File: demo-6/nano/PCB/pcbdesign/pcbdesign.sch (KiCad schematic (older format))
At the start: 18 parts, among them J1 Relay, J2 12v input, J3 Encoder, J4 HC-SR04, J5 Display, J6 InflowPump, J7 Outflow Switch, J8 Outflow Pump, Q1 PN2222A

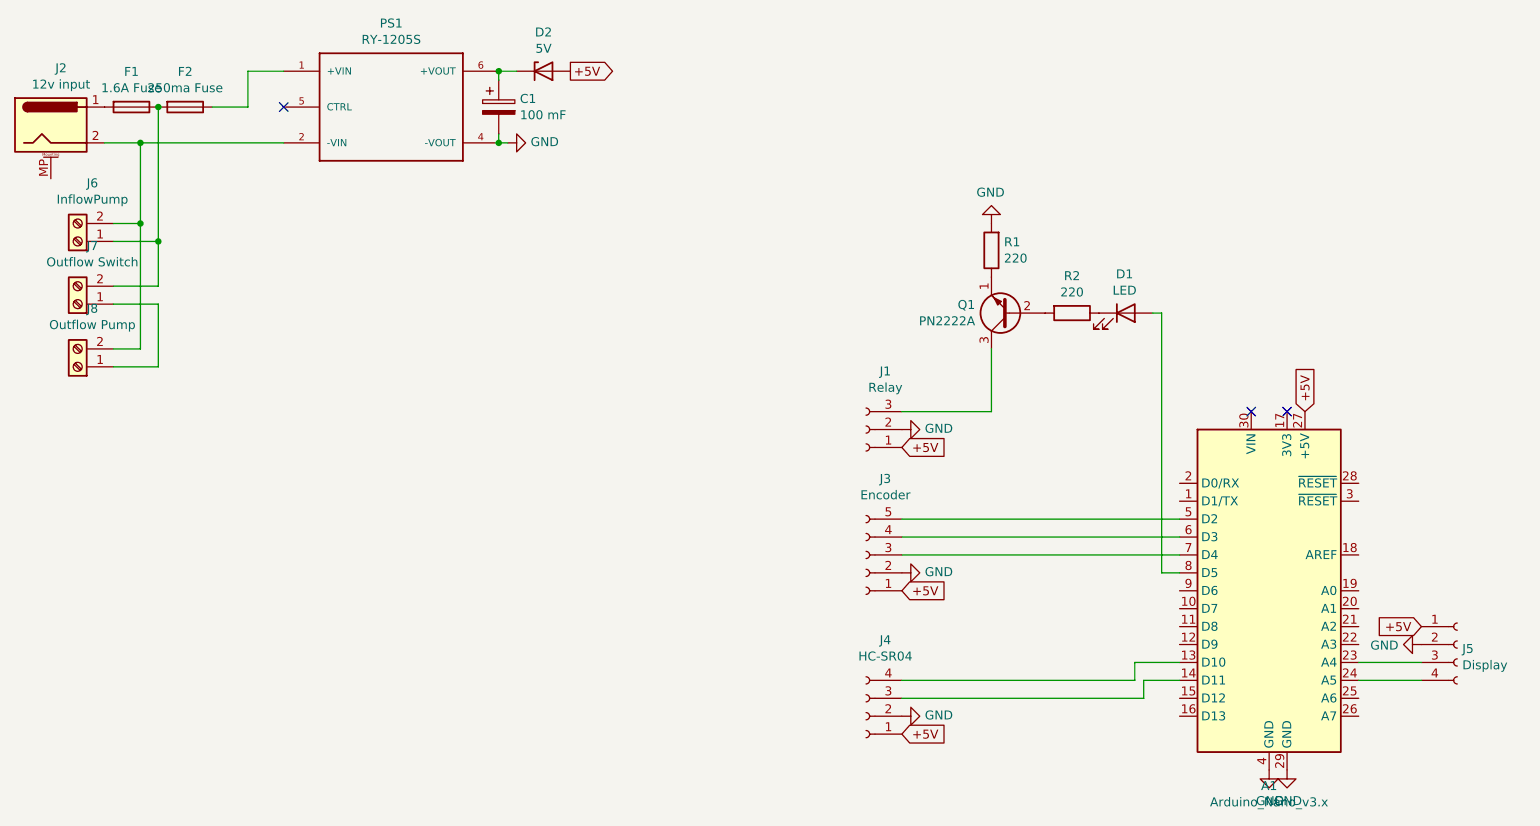
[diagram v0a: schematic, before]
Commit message: adding some schematics
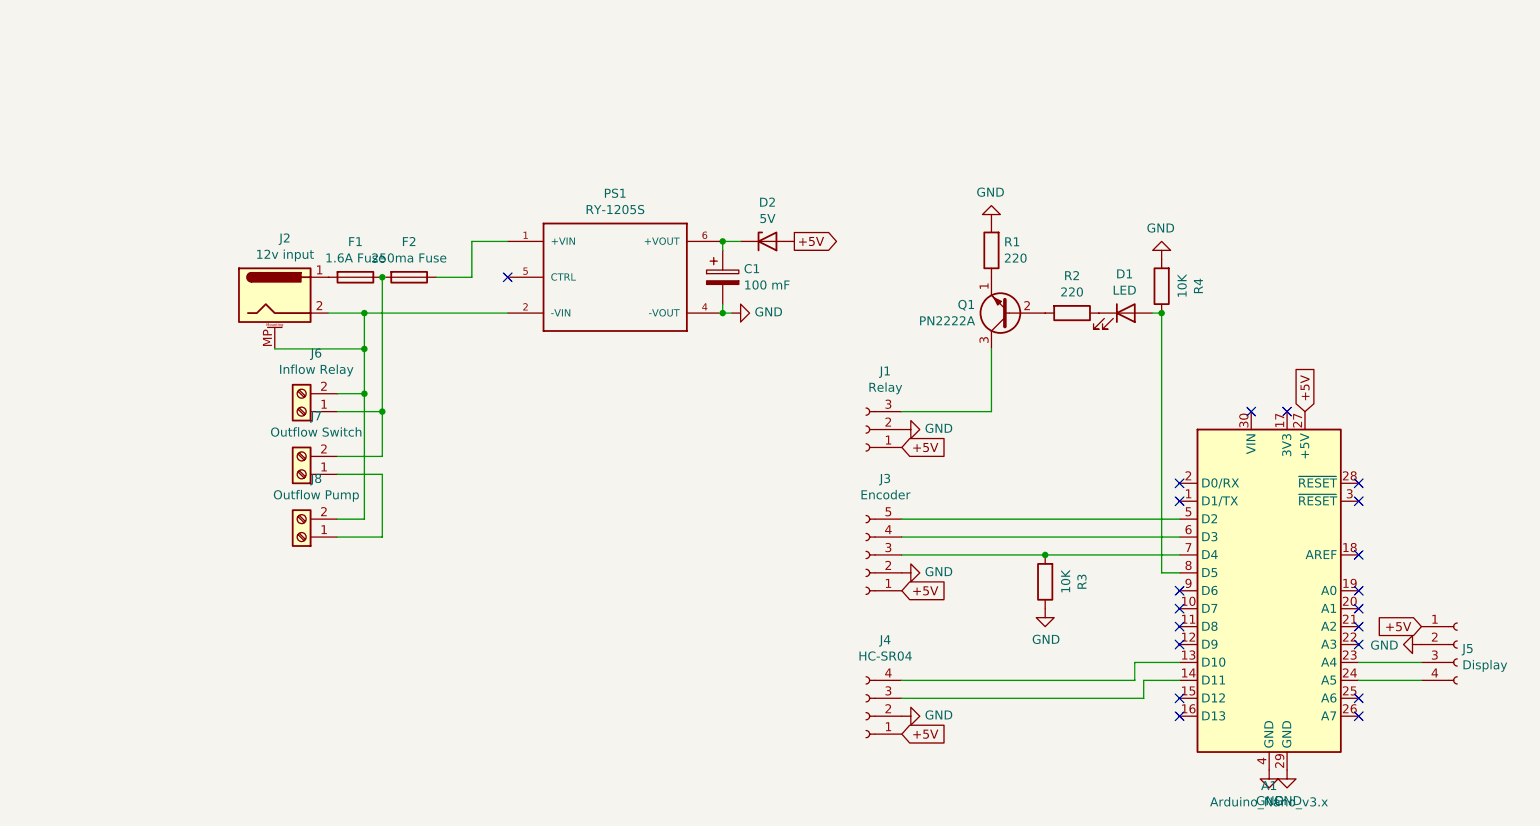
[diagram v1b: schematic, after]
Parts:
- added R3, R4: 10K, Resistor_THT:R_Axial_DIN0207_L6.3mm_D2.5mm_P7.62mm_Horizontal, symbol Device:R
- C1: footprint (none) -> Capacitor_THT:CP_Radial_D8.0mm_P3.50mm
- D1: footprint (none) -> LED_THT:LED_D4.0mm
- D2: footprint (none) -> Diode_THT:D_A-405_P7.62mm_Horizontal
- F1, F2: footprint (none) -> Fuse:Fuseholder_Cylinder-6.3x32mm_Schurter_0031-8002_Horizontal_Open
- J1: footprint (none) -> Connector_PinSocket_2.54mm:PinSocket_1x03_P2.54mm_Vertical
- J4, J5: footprint (none) -> Connector_PinSocket_2.54mm:PinSocket_1x04_P2.54mm_Vertical
- J6: value InflowPump -> Inflow Relay; footprint (none) -> TerminalBlock:TerminalBlock_bornier-2_P5.08mm
- J7, J8: footprint (none) -> TerminalBlock:TerminalBlock_bornier-2_P5.08mm
- PS1: footprint CONV_RY-1205S -> RY-1205S:CONV_RY-1205S
- R1, R2: footprint (none) -> Resistor_THT:R_Axial_DIN0207_L6.3mm_D2.5mm_P7.62mm_Horizontal
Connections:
- net GND: now also R3.1, R4.2
- net at A1.7 (D4), J3.3 (Pin_3): now also R3.2
- net at A1.8 (D5), D1.2 (A): now also R4.1
- net at J2.2, J6.2 (Pin_2), J8.2 (Pin_2)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: now also J2.MP (MountPin)
- no-connect marks 3 -> 20
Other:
- moved on the sheet: C1, D2, F1, F2, J2, J6, J7, J8

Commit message: ready for pcb
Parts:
- J2: footprint Connector_BarrelJack:BarrelJack_Wuerth_6941xx301002 -> Connector_BarrelJack:BarrelJack_CUI_PJ-063AH_Horizontal
- J3: footprint Connector_BarrelJack:BarrelJack_Horizontal -> Connector_PinSocket_2.54mm:PinSocket_1x05_P2.54mm_Vertical
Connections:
- net at A1.8 (D5), D1.2 (A): no longer R4.1
- net at D1.1 (K), R2.1: now also R4.1
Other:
- moved on the sheet: R4
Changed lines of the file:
@@
 F 0 "J3" H 6142 3475 50  0000 C CNN
 F 1 "Encoder" H 6142 3566 50  0000 C CNN
-F 2 "Connector_BarrelJack:BarrelJack_Horizontal" H 6250 3900 50  0001 C CNN
+F 2 "Connector_PinSocket_2.54mm:PinSocket_1x05_P2.54mm_Vertical" H 6250 3900 50  0001 C CNN
 F 3 "~" H 6250 3900 50  0001 C CNN
 	1    6250 3900
@@
 	0    -1   -1   0
 $EndComp
-$Comp
-L Connector:Conn_01x04_Female J5
-U 1 1 5F4E310F
-P 9550 4400
-F 0 "J5" H 9578 4376 50  0000 L CNN
-F 1 "Display" H 9578 4285 50  0000 L CNN
-F 2 "Connector_PinSocket_2.54mm:PinSocket_1x04_P2.54mm_Vertical" H 9550 4400 50  0001 C CNN
-F 3 "~" H 9550 4400 50  0001 C CNN
-	1    9550 4400
-	1    0    0    -1
-$EndComp
 Wire Wire Line
 	9350 4600 9000 4600
@@
 F 0 "J2" H 3007 2767 50  0000 C CNN
 F 1 "12v input" H 3007 2676 50  0000 C CNN
-F 2 "Connector_BarrelJack:BarrelJack_Wuerth_6941xx301002" H 3000 2410 50  0001 C CNN
+F 2 "Connector_BarrelJack:BarrelJack_CUI_PJ-063AH_Horizontal" H 3000 2410 50  0001 C CNN
 F 3 "~" H 3000 2410 50  0001 C CNN
 	1    2950 2450
@@
 L power:GND #PWR03
 U 1 1 5F4E5570
-P 7900 2250
-F 0 "#PWR03" H 7900 2000 50  0001 C CNN
-F 1 "GND" H 7905 2077 50  0000 C CNN
-F 2 "" H 7900 2250 50  0001 C CNN
-F 3 "" H 7900 2250 50  0001 C CNN
-	1    7900 2250
-	-1   0    0    1
-$EndComp
-Connection ~ 7900 2550
+P 7550 2250
+F 0 "#PWR03" H 7550 2000 50  0001 C CNN
+F 1 "GND" H 7555 2077 50  0000 C CNN
+F 2 "" H 7550 2250 50  0001 C CNN
+F 3 "" H 7550 2250 50  0001 C CNN
+	1    7550 2250
+	-1   0    0    1
+$EndComp
 $Comp
 L Device:R R4
 U 1 1 5F4E50D6
-P 7900 2400
-F 0 "R4" V 7693 2400 50  0000 C CNN
-F 1 "10K" V 7784 2400 50  0000 C CNN
-F 2 "Resistor_THT:R_Axial_DIN0207_L6.3mm_D2.5mm_P7.62mm_Horizontal" V 7830 2400 50  0001 C CNN
-F 3 "~" H 7900 2400 50  0001 C CNN
-	1    7900 2400
+P 7550 2400
+F 0 "R4" V 7343 2400 50  0000 C CNN
+F 1 "10K" V 7434 2400 50  0000 C CNN
+F 2 "Resistor_THT:R_Axial_DIN0207_L6.3mm_D2.5mm_P7.62mm_Horizontal" V 7480 2400 50  0001 C CNN
+F 3 "~" H 7550 2400 50  0001 C CNN
+	1    7550 2400
 	-1   0    0    1
 $EndComp
@@
 Connection ~ 5450 2150
 Connection ~ 5450 2550
+Connection ~ 7550 2550
+$Comp
+L Connector:Conn_01x04_Female J5
+U 1 1 5F4E310F
+P 9550 4400
+F 0 "J5" H 9578 4376 50  0000 L CNN
+F 1 "Display" H 9578 4285 50  0000 L CNN
+F 2 "Connector_PinSocket_2.54mm:PinSocket_1x04_P2.54mm_Vertical" H 9550 4400 50  0001 C CNN
+F 3 "~" H 9550 4400 50  0001 C CNN
+	1    9550 4400
+	1    0    0    -1
+$EndComp
 $EndSCHEMATC
